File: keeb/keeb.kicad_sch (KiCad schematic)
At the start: 162 parts, among them J101 USB_C_Receptacle_USB2.0, J102 AVR-ISP-6, SW101 SW_Push, SW102 SW_Push, SW103 SW_Push, SW104 SW_Push, SW105 SW_Push, SW106 SW_Push, SW107 SW_Push, SW108 SW_Push, SW109 SW_Push, SW110 SW_Push, SW111 SW_Push, SW112 SW_Push, SW113 SW_Push, SW114 SW_Push, SW115 SW_Push, SW116 SW_Push, SW117 SW_Push, SW118 SW_Push, SW119 SW_Push, SW120 SW_Push, SW121 SW_Push, SW122 SW_Push, SW123 SW_Push, SW124 SW_Push, SW125 SW_Push, SW126 SW_Push, SW127 SW_Push, SW128 SW_Push, SW129 SW_Push, SW130 SW_Push, SW131 SW_Push, SW132 SW_Push, SW133 SW_Push, SW134 SW_Push, SW135 SW_Push, SW136 SW_Push, SW137 SW_Push, SW138 SW_Push, SW139 SW_Push, SW140 SW_Push, SW141 SW_Push, SW142 SW_Push, SW143 SW_Push, SW144 SW_Push, SW145 SW_Push, SW146 SW_Push, SW147 SW_Push, SW148 SW_Push, SW149 SW_Push, SW150 SW_Push, SW151 SW_Push, SW152 SW_Push, SW153 SW_Push, SW154 SW_Push, SW155 SW_Push, SW156 SW_Push, SW157 SW_Push, SW158 SW_Push, SW159 SW_Push, SW160 SW_Push, SW161 SW_Push, SW162 SW_Push, SW163 SW_Push, SW164 SW_Push, SW165 SW_Push, SW166 SW_Push, SW167 SW_Push, U101 TPD2S017, U102 ATmega32U4-AU, Y101 16Mhz

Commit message: layout cont, fp mcu updated
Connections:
- net COL_3: now also U102.31 (PC6); no longer U102.12 (PB7)
- net COL_4: now also U102.32 (PC7); no longer U102.31 (PC6)
- net COL_5: now also U102.36 (PF7); no longer U102.32 (PC7)

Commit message: footprints, part selection, cleanupo
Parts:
- C101: renamed from C104; value 10u -> 1u; footprint Capacitor_SMD:C_1206_3216Metric_Pad1.33x1.80mm_HandSolder -> Capacitor_SMD:C_0603_1608Metric; LCSC # (none) -> C15849; LCSC Link (none) -> https://datasheet.lcsc.com/lcsc/1810261812_Samsung-Electro-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
- C102: renamed from C105; LCSC # (none) -> C1525; LCSC Link (none) -> https://www.lcsc.com/product-detail/Multilayer-Ceramic-Capa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
- C103: renamed from C106; LCSC # (none) -> C1525; LCSC Link (none) -> https://www.lcsc.com/product-detail/Multilayer-Ceramic-Capa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
- C104: renamed from C107; LCSC # (none) -> C1525; LCSC Link (none) -> https://www.lcsc.com/product-detail/Multilayer-Ceramic-Capa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
- C105: renamed from C108; LCSC # (none) -> C1525; LCSC Link (none) -> https://www.lcsc.com/product-detail/Multilayer-Ceramic-Capa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
- C106: renamed from C109; LCSC # (none) -> C1525; LCSC Link (none) -> https://www.lcsc.com/product-detail/Multilayer-Ceramic-Capa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
- C107: renamed from C103; footprint Capacitor_SMD:C_0402_1005Metric -> Capacitor_SMD:C_0603_1608Metric; LCSC # (none) -> C15849; LCSC Link (none) -> https://datasheet.lcsc.com/lcsc/1810261812_Samsung-Electro-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
- D101, D102, D103, D104, D105, D106, D107, D108, D109, D110, D111, D112, D113, D114, D115, D116, D117, D118, D119, D120, D121, D122, D123, D124, D125, D126, D127, D128, D129, D130, D131, D132, D133, D134, D135, D136, D137, D138, D139, D140, D141, D142, D143, D144, D145, D146, D147, D148, D149, D150, D151, D152, D153, D154, D155, D156, D157, D158, D159, D160, D161, D162, D163, D164, D165, D166: footprint Diode_SMD:D_SOD-323F -> Diode_SMD:D_SOD-123F; LCSC # (none) -> C64898; LCSC Link (none) -> https://www.lcsc.com/product-detail/Diodes---General-Purpos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
- F101: footprint Fuse:Fuse_1206_3216Metric_Pad1.42x1.75mm_HandSolder -> Fuse:Fuse_0603_1608Metric; LCSC # (none) -> C369159; LCSC Link (none) -> https://www.lcsc.com/product-detail/Resettable-Fuses_Jinrui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
- I2C_101, I2C_102: LCSC # (none) -> C388632; LCSC Link (none) -> https://www.lcsc.com/product-detail/Audio-Connectors_XKB-Co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; Supplier # digi: 839-54-00177CT-ND -> (none)
- J102: renamed from J101; LCSC # (none) -> C165948; LCSC Link (none) -> https://www.lcsc.com/product-detail/USB-Connectors_Korean-H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; Supplier # LCSC: C165948 -> (none)
- SW167: LCSC # (none) -> C231329; LCSC Link (none) -> https://www.lcsc.com/product-detail/Tactile-Switches_Omron-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; Supplier # LCSC: C231329 -> (none)
- U101: LCSC # (none) -> C880115; LCSC Link (none) -> https://www.lcsc.com/product-detail/ESD-Protection-Devices_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
- U102: value ATmega32U4-AU -> ATmega32U4-MU; LCSC # (none) -> C112161; LCSC Link (none) -> https://www.lcsc.com/product-detail/Microcontroller-Units-M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; Supplier # digi: ATMEGA32U4RC-AU-ND -> (none)
- Y101: LCSC https://www.lcsc.com/product-detail/Crystals_YLFailong-Crys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 -> (none); LCSC # (none) -> C431146; LCSC Link (none) -> https://www.lcsc.com/product-detail/Crystals_YLFailong-Crys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; LCSC# C431146 -> (none)
- renumbered C101 to C108, C102 to C109, J102 to J101
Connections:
- net +5V: now also U101.5 (VCC)
- net VBUS: no longer U101.5 (VCC)
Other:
- moved on the sheet: C101, C102, C103, C104, C105, C106, C107, C108, C109, F101, I2C_101, J101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

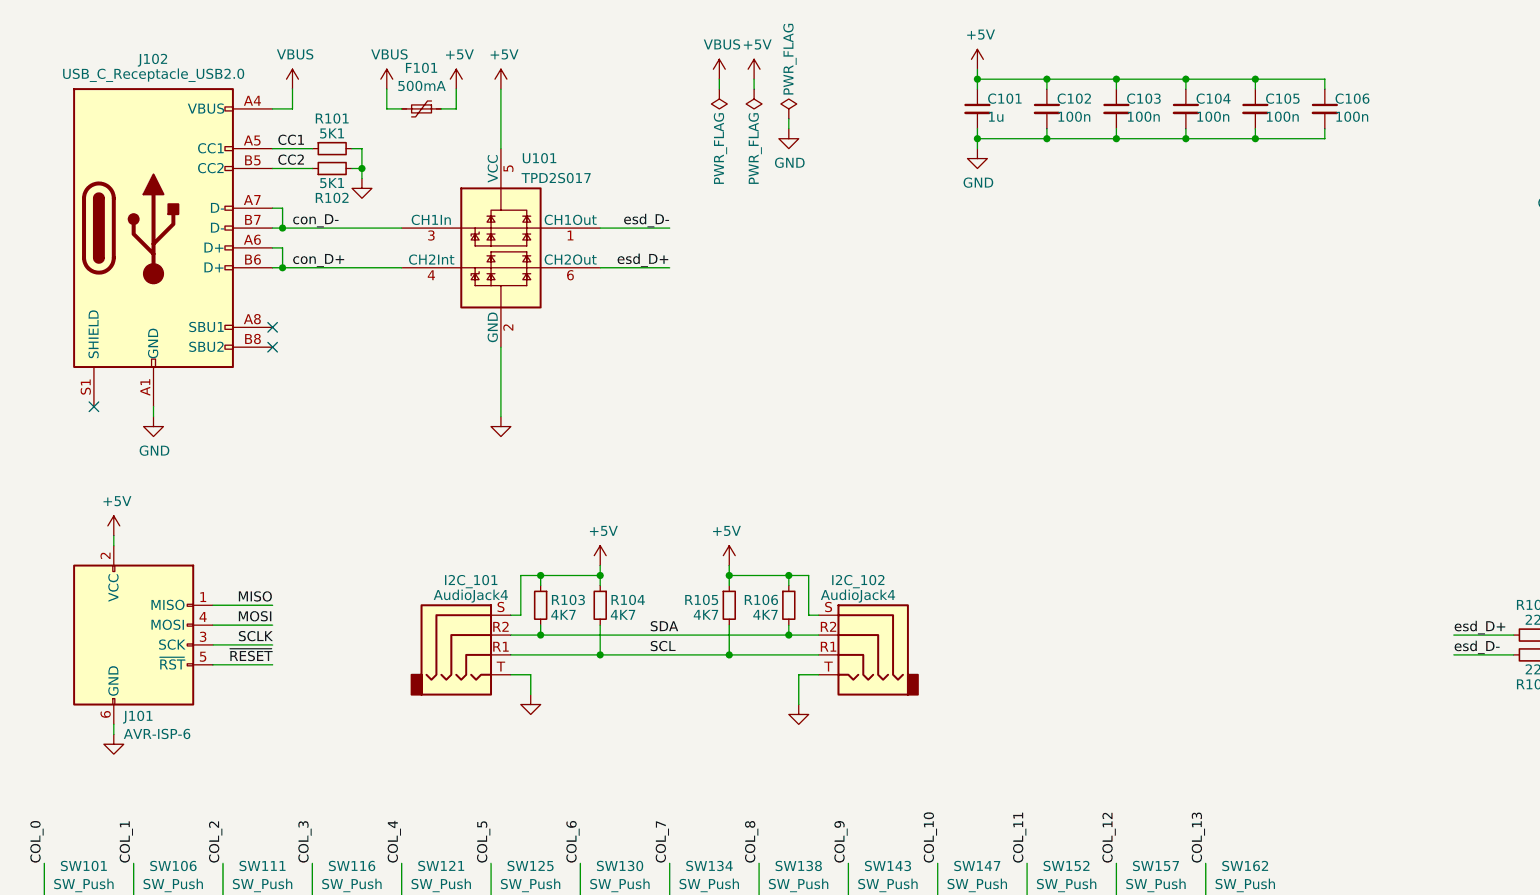
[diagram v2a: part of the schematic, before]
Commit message: row and col via and trace spacing and fillets
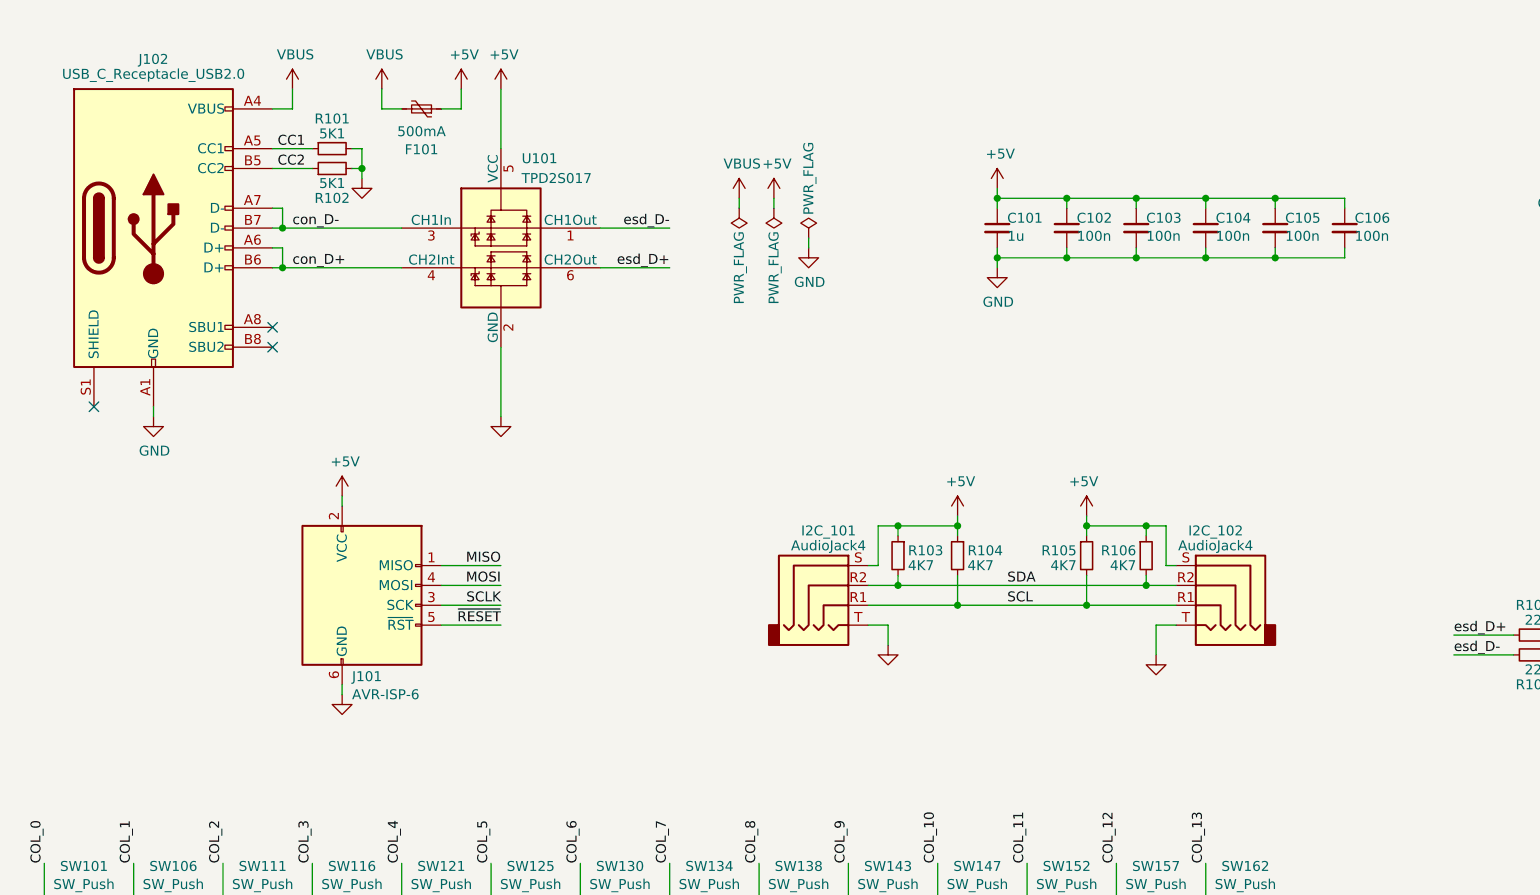
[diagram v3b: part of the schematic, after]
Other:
- moved on the sheet: C101, C102, C103, C104, C105, C106, I2C_101, I2C_102, J101, R103, R104, R105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

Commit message: LCSC part selected
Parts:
- C108, C109: LCSC # (none) -> C1555; LCSC Link (none) -> https://www.lcsc.com/product-detail/Multilayer-Ceramic-Capa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
- R101, R102: LCSC # (none) -> C25905; LCSC Link (none) -> https://www.lcsc.com/product-detail/Chip-Resistor---Surface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
- R103, R104, R105, R106: LCSC # (none) -> C25900; LCSC Link (none) -> https://www.lcsc.com/product-detail/Chip-Resistor---Surface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
- R107, R108: LCSC # (none) -> C25092; LCSC Link (none) -> https://www.lcsc.com/product-detail/Chip-Resistor---Surface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
- R109, R110: LCSC # (none) -> C25744; LCSC Link (none) -> https://www.lcsc.com/product-detail/Chip-Resistor---Surface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
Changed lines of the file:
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@@
       (effects (font (size 1.27 1.27)) hide)
     )
-    (property "Datasheet" "~" (at 207.01 92.71 0)
+    (property "Datasheet" "https://datasheet.lcsc.com/lcsc/2205311900_UNI-ROYAL-Uniroyal-Elec-0402WGF220JTCE_C25092.pdf" (at 207.01 92.71 0)
+      (effects (font (size 1.27 1.27)) hide)
+    )
+    (property "LCSC #" "C25092" (at 207.01 92.71 0)
+      (effects (font (size 1.27 1.27)) hide)
+    )
+    (property "LCSC Link" "https://www.lcsc.com/product-detail/Chip-Resistor---Surface-Mount_UNI-ROYALUniroyal-Elec-UNI-ROYALUniroyal-Elec-0402WGF220JTCE_C25092.html" (at 207.01 92.71 0)
       (effects (font (size 1.27 1.27)) hide)
     )
@@
       (effects (font (size 1.27 1.27)) hide)
     )
-    (property "Datasheet" "~" (at 207.01 95.25 0)
+    (property "Datasheet" "https://datasheet.lcsc.com/lcsc/2205311900_UNI-ROYAL-Uniroyal-Elec-0402WGF220JTCE_C25092.pdf" (at 207.01 95.25 0)
+      (effects (font (size 1.27 1.27)) hide)
+    )
+    (property "LCSC #" "C25092" (at 207.01 95.25 0)
+      (effects (font (size 1.27 1.27)) hide)
+    )
+    (property "LCSC Link" "https://www.lcsc.com/product-detail/Chip-Resistor---Surface-Mount_UNI-ROYALUniroyal-Elec-UNI-ROYALUniroyal-Elec-0402WGF220JTCE_C25092.html" (at 207.01 95.25 0)
       (effects (font (size 1.27 1.27)) hide)
     )
@@
       (effects (font (size 1.27 1.27)) hide)
     )
-    (property "Datasheet" "" (at 125.73 82.55 0)
+    (property "Datasheet" "https://datasheet.lcsc.com/lcsc/2206010045_UNI-ROYAL-Uniroyal-Elec-0402WGF4701TCE_C25900.pdf" (at 125.73 82.55 0)
+      (effects (font (size 1.27 1.27)) hide)
+    )
+    (property "LCSC #" "C25900" (at 125.73 82.55 0)
+      (effects (font (size 1.27 1.27)) hide)
+    )
+    (property "LCSC Link" "https://www.lcsc.com/product-detail/Chip-Resistor---Surface-Mount_UNI-ROYALUniroyal-Elec-UNI-ROYALUniroyal-Elec-0402WGF4701TCE_C25900.html" (at 125.73 82.55 0)
       (effects (font (size 1.27 1.27)) hide)
     )
@@
       (effects (font (size 1.27 1.27)) hide)
     )
-    (property "Datasheet" "~" (at 53.34 33.02 0)
+    (property "Datasheet" "https://datasheet.lcsc.com/lcsc/2206010045_UNI-ROYAL-Uniroyal-Elec-0402WGF5101TCE_C25905.pdf" (at 53.34 33.02 0)
+      (effects (font (size 1.27 1.27)) hide)
+    )
+    (property "LCSC #" "C25905" (at 53.34 33.02 0)
+      (effects (font (size 1.27 1.27)) hide)
+    )
+    (property "LCSC Link" "https://www.lcsc.com/product-detail/Chip-Resistor---Surface-Mount_UNI-ROYALUniroyal-Elec-UNI-ROYALUniroyal-Elec-0402WGF5101TCE_C25905.html" (at 53.34 33.02 0)
       (effects (font (size 1.27 1.27)) hide)
     )
@@
       (effects (font (size 1.27 1.27)) hide)
     )
-    (property "Datasheet" "~" (at 53.34 30.48 0)
+    (property "Datasheet" "https://datasheet.lcsc.com/lcsc/2206010045_UNI-ROYAL-Uniroyal-Elec-0402WGF5101TCE_C25905.pdf" (at 53.34 30.48 0)
+      (effects (font (size 1.27 1.27)) hide)
+    )
+    (property "LCSC #" "C25905" (at 53.34 30.48 0)
+      (effects (font (size 1.27 1.27)) hide)
+    )
+    (property "LCSC Link" "https://www.lcsc.com/product-detail/Chip-Resistor---Surface-Mount_UNI-ROYALUniroyal-Elec-UNI-ROYALUniroyal-Elec-0402WGF5101TCE_C25905.html" (at 53.34 30.48 0)
       (effects (font (size 1.27 1.27)) hide)
     )
@@
       (effects (font (size 1.27 1.27)) hide)
     )
-    (property "Datasheet" "~" (at 214.63 38.1 0)
+    (property "Datasheet" "https://datasheet.lcsc.com/lcsc/1811141710_FH--Guangdong-Fenghua-Advanced-Tech-0402CG220J500NT_C1555.pdf" (at 214.63 38.1 0)
+      (effects (font (size 1.27 1.27)) hide)
+    )
+    (property "LCSC #" "C1555" (at 214.63 38.1 0)
+      (effects (font (size 1.27 1.27)) hide)
+    )
+    (property "LCSC Link" "https://www.lcsc.com/product-detail/Multilayer-Ceramic-Capacitors-MLCC---SMD-SMT_FH-Guangdong-Fenghua-Advanced-Tech-FH-Guangdong-Fenghua-Advanced-Tech-0402CG220J500NT_C1555.html" (at 214.63 38.1 0)
       (effects (font (size 1.27 1.27)) hide)
     )
@@
       (effects (font (size 1.27 1.27)) hide)
     )
-    (property "Datasheet" "~" (at 226.06 38.1 0)
+    (property "Datasheet" "https://datasheet.lcsc.com/lcsc/1811141710_FH--Guangdong-Fenghua-Advanced-Tech-0402CG220J500NT_C1555.pdf" (at 226.06 38.1 0)
+      (effects (font (size 1.27 1.27)) hide)
+    )
+    (property "LCSC #" "C1555" (at 226.06 38.1 0)
+      (effects (font (size 1.27 1.27)) hide)
+    )
+    (property "LCSC Link" "https://www.lcsc.com/product-detail/Multilayer-Ceramic-Capacitors-MLCC---SMD-SMT_FH-Guangdong-Fenghua-Advanced-Tech-FH-Guangdong-Fenghua-Advanced-Tech-0402CG220J500NT_C1555.html" (at 226.06 38.1 0)
       (effects (font (size 1.27 1.27)) hide)
     )
@@
       (effects (font (size 1.27 1.27)) hide)
     )
-    (property "Datasheet" "~" (at 256.54 35.56 0)
+    (property "Datasheet" "https://datasheet.lcsc.com/lcsc/2206010100_UNI-ROYAL-Uniroyal-Elec-0402WGF1002TCE_C25744.pdf" (at 256.54 35.56 0)
+      (effects (font (size 1.27 1.27)) hide)
+    )
+    (property "LCSC #" "C25744" (at 256.54 35.56 0)
+      (effects (font (size 1.27 1.27)) hide)
+    )
+    (property "LCSC Link" "https://www.lcsc.com/product-detail/Chip-Resistor---Surface-Mount_UNI-ROYALUniroyal-Elec-UNI-ROYALUniroyal-Elec-0402WGF1002TCE_C25744.html" (at 256.54 35.56 0)
       (effects (font (size 1.27 1.27)) hide)
     )
@@
       (effects (font (size 1.27 1.27)) hide)
     )
-    (property "Datasheet" "~" (at 245.11 36.83 0)
+    (property "Datasheet" "https://datasheet.lcsc.com/lcsc/2206010100_UNI-ROYAL-Uniroyal-Elec-0402WGF1002TCE_C25744.pdf" (at 245.11 36.83 0)
+      (effects (font (size 1.27 1.27)) hide)
+    )
+    (property "LCSC #" "C25744" (at 245.11 36.83 0)
+      (effects (font (size 1.27 1.27)) hide)
+    )
+    (property "LCSC Link" "https://www.lcsc.com/product-detail/Chip-Resistor---Surface-Mount_UNI-ROYALUniroyal-Elec-UNI-ROYALUniroyal-Elec-0402WGF1002TCE_C25744.html" (at 245.11 36.83 0)
       (effects (font (size 1.27 1.27)) hide)
     )
@@
       (effects (font (size 1.27 1.27)) hide)
     )
-    (property "Datasheet" "" (at 157.48 82.55 0)
+    (property "Datasheet" "https://datasheet.lcsc.com/lcsc/2206010045_UNI-ROYAL-Uniroyal-Elec-0402WGF4701TCE_C25900.pdf" (at 157.48 82.55 0)
+      (effects (font (size 1.27 1.27)) hide)
+    )
+    (property "LCSC #" "C25900" (at 157.48 82.55 0)
+      (effects (font (size 1.27 1.27)) hide)
+    )
+    (property "LCSC Link" "https://www.lcsc.com/product-detail/Chip-Resistor---Surface-Mount_UNI-ROYALUniroyal-Elec-UNI-ROYALUniroyal-Elec-0402WGF4701TCE_C25900.html" (at 157.48 82.55 0)
       (effects (font (size 1.27 1.27)) hide)
     )
@@
       (effects (font (size 1.27 1.27)) hide)
     )
-    (property "Datasheet" "" (at 133.35 82.55 0)
+    (property "Datasheet" "https://datasheet.lcsc.com/lcsc/2206010045_UNI-ROYAL-Uniroyal-Elec-0402WGF4701TCE_C25900.pdf" (at 133.35 82.55 0)
+      (effects (font (size 1.27 1.27)) hide)
+    )
+    (property "LCSC #" "C25900" (at 133.35 82.55 0)
+      (effects (font (size 1.27 1.27)) hide)
+    )
+    (property "LCSC Link" "https://www.lcsc.com/product-detail/Chip-Resistor---Surface-Mount_UNI-ROYALUniroyal-Elec-UNI-ROYALUniroyal-Elec-0402WGF4701TCE_C25900.html" (at 133.35 82.55 0)
       (effects (font (size 1.27 1.27)) hide)
     )
@@
       (effects (font (size 1.27 1.27)) hide)
     )
-    (property "Datasheet" "" (at 149.86 82.55 0)
+    (property "Datasheet" "https://datasheet.lcsc.com/lcsc/2206010045_UNI-ROYAL-Uniroyal-Elec-0402WGF4701TCE_C25900.pdf" (at 149.86 82.55 0)
+      (effects (font (size 1.27 1.27)) hide)
+    )
+    (property "LCSC #" "C25900" (at 149.86 82.55 0)
+      (effects (font (size 1.27 1.27)) hide)
+    )
+    (property "LCSC Link" "https://www.lcsc.com/product-detail/Chip-Resistor---Surface-Mount_UNI-ROYALUniroyal-Elec-UNI-ROYALUniroyal-Elec-0402WGF4701TCE_C25900.html" (at 149.86 82.55 0)
       (effects (font (size 1.27 1.27)) hide)
     )

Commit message: all FP cleaned up and updated
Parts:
- C101, C107: footprint Capacitor_SMD:C_0603_1608Metric -> unORTHOdox:C_0603_1608Metric
- C102, C103, C104, C105, C106, C108, C109: footprint Capacitor_SMD:C_0402_1005Metric -> unORTHOdox:C_0402_1005Metric
- D101, D102, D103, D104, D105, D106, D107, D108, D109, D110, D111, D112, D113, D114, D115, D116, D117, D118, D119, D120, D121, D122, D123, D124, D125, D126, D127, D128, D129, D130, D131, D132, D133, D134, D135, D136, D137, D138, D139, D140, D141, D142, D143, D144, D145, D146, D147, D148, D149, D150, D151, D152, D153, D154, D155, D156, D157, D158, D159, D160, D161, D162, D163, D164, D165, D166: footprint Diode_SMD:D_SOD-123F -> unORTHOdox:D_SOD-123F
- F101: footprint Fuse:Fuse_0603_1608Metric -> unORTHOdox:Fuse_0603_1608Metric
- R101, R102, R103, R104, R105, R106, R107, R108, R109, R110: footprint Resistor_SMD:R_0402_1005Metric -> unORTHOdox:R_0402_1005Metric
- SW167: footprint Button_Switch_SMD:SW_SPST_B3U-1000P -> unORTHOdox:SW_SPST_B3U-1000P
- U101: footprint Package_TO_SOT_SMD:SOT-23-6 -> unORTHOdox:SOT-23-6
- Y101: footprint Crystal:Crystal_SMD_2016-4Pin_2.0x1.6mm -> unORTHOdox:Crystal_SMD_2016-4Pin_2.0x1.6mm
